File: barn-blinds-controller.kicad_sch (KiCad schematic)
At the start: 4 parts

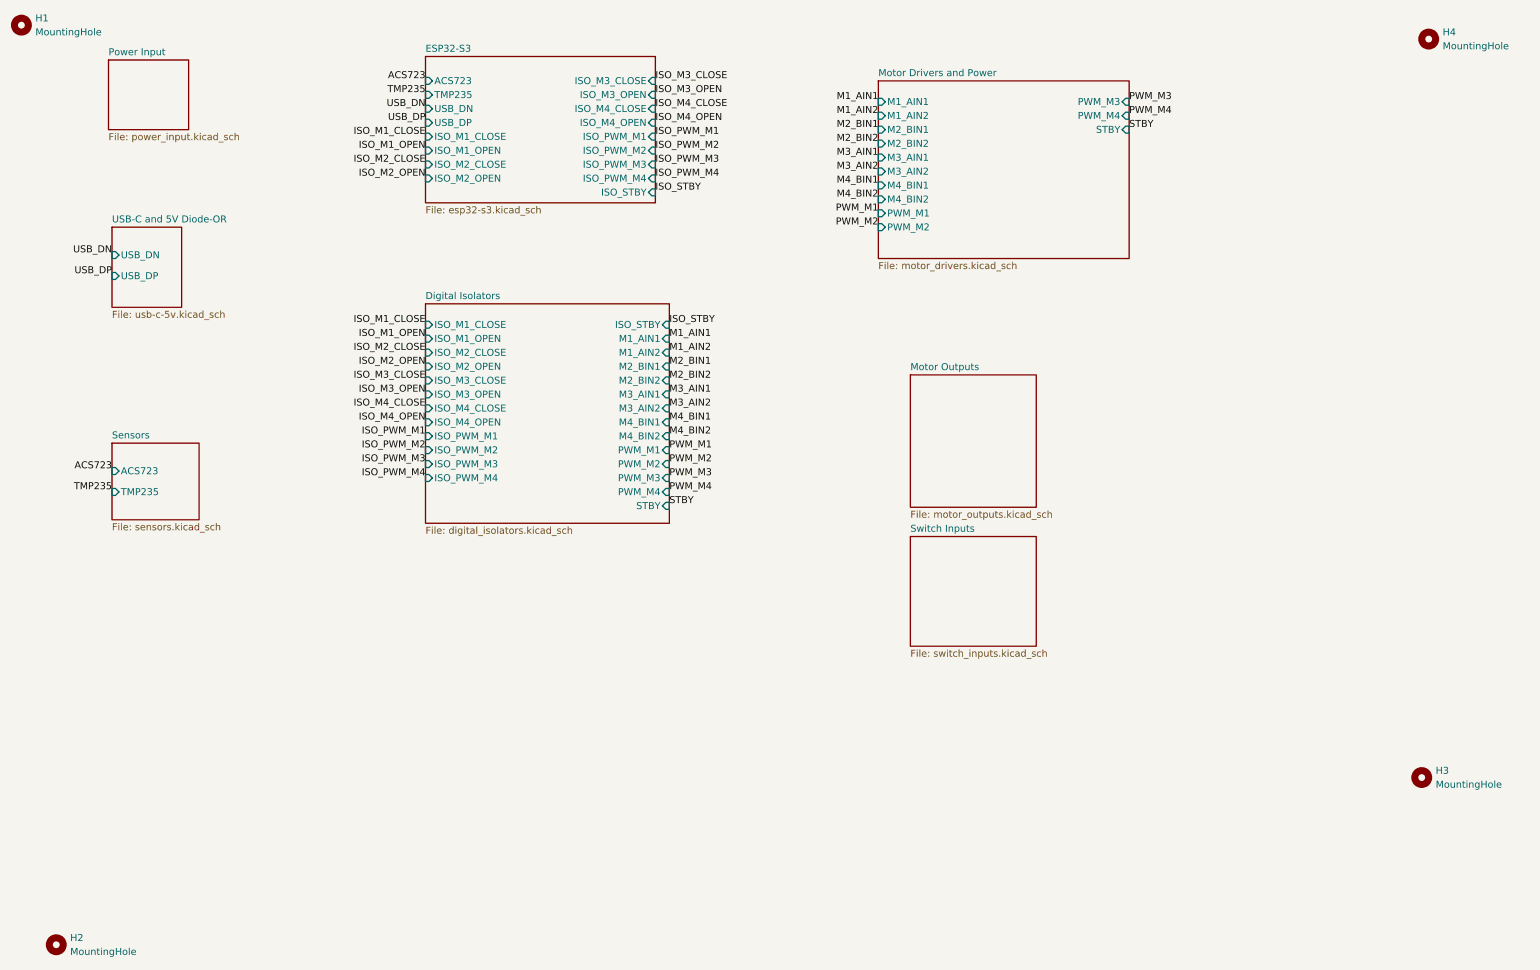
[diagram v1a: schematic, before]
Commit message: Updating routing with new terminal block
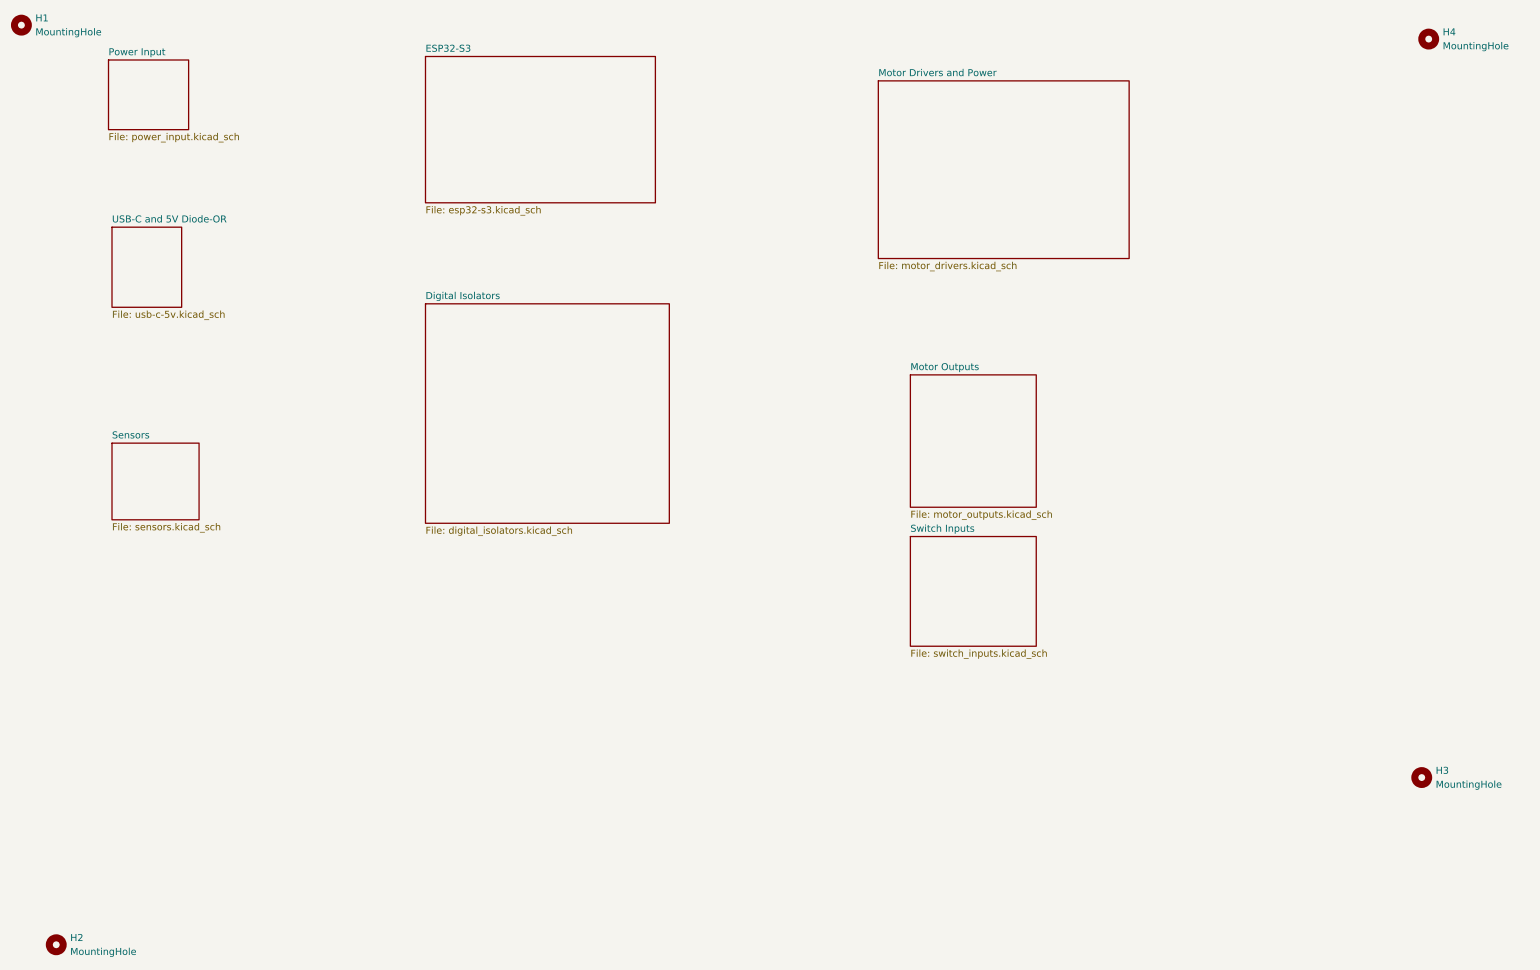
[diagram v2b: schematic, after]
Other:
- sheet Digital Isolators ports: added none; removed ISO_M1_CLOSE, ISO_M1_OPEN, ISO_M2_CLOSE, ISO_M2_OPEN, ISO_M3_CLOSE, ISO_M3_OPEN, ISO_M4_CLOSE, ISO_M4_OPEN, ISO_PWM_M1, ISO_PWM_M2, ISO_PWM_M3, ISO_PWM_M4, ISO_STBY, M1_AIN1, M1_AIN2, M2_BIN1, M2_BIN2, M3_AIN1, M3_AIN2, M4_BIN1, M4_BIN2, PWM_M1, PWM_M2, PWM_M3, PWM_M4, STBY
- sheet ESP32-S3 ports: added none; removed ACS723, ISO_M1_CLOSE, ISO_M1_OPEN, ISO_M2_CLOSE, ISO_M2_OPEN, ISO_M3_CLOSE, ISO_M3_OPEN, ISO_M4_CLOSE, ISO_M4_OPEN, ISO_PWM_M1, ISO_PWM_M2, ISO_PWM_M3, ISO_PWM_M4, ISO_STBY, TMP235, USB_DN, USB_DP
- sheet Motor Drivers and Power ports: added none; removed M1_AIN1, M1_AIN2, M2_BIN1, M2_BIN2, M3_AIN1, M3_AIN2, M4_BIN1, M4_BIN2, PWM_M1, PWM_M2, PWM_M3, PWM_M4, STBY
- sheet Sensors ports: added none; removed ACS723, TMP235
- sheet USB-C and 5V Diode-OR ports: added none; removed USB_DN, USB_DP
